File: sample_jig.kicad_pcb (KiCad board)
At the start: 2 copper layers, 50 x 50 mm, 25 parts

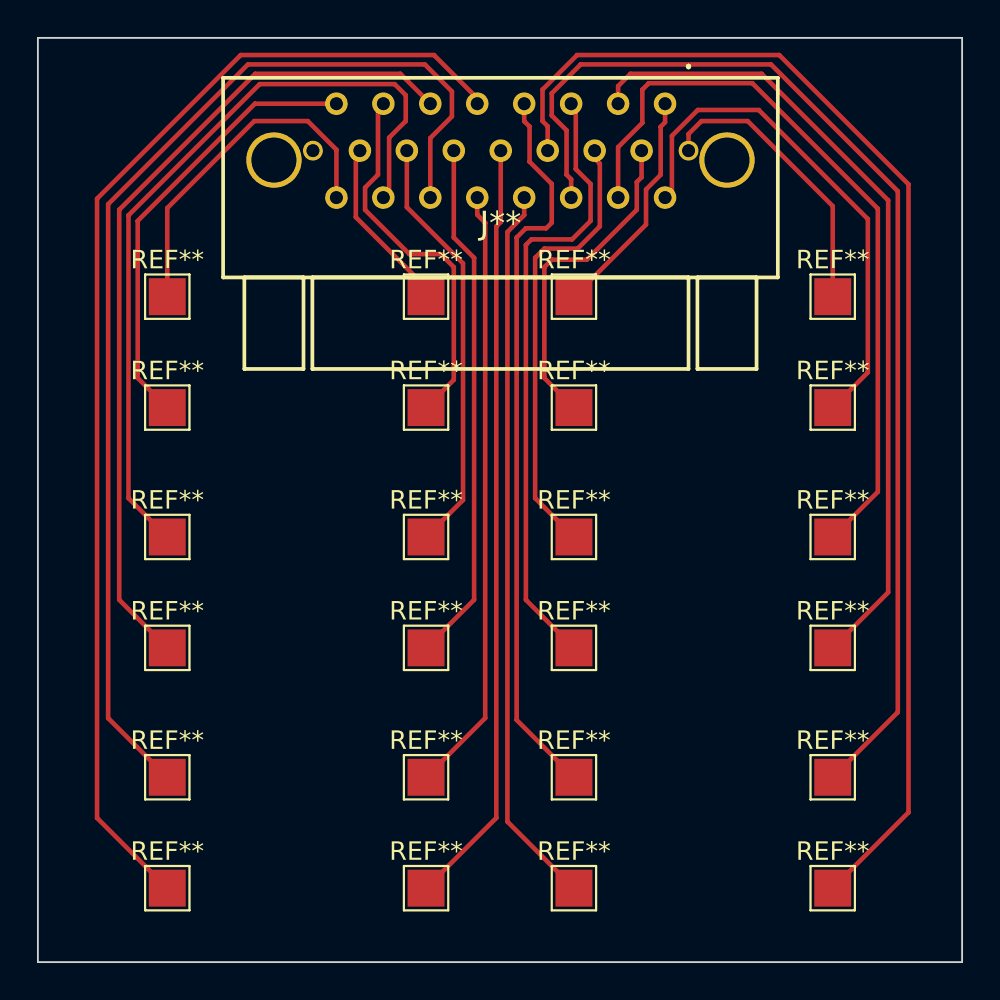
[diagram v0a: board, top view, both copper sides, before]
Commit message: running into some problems with pcb potentially, need to decide if this design will work or to do the more traditional flexing design.
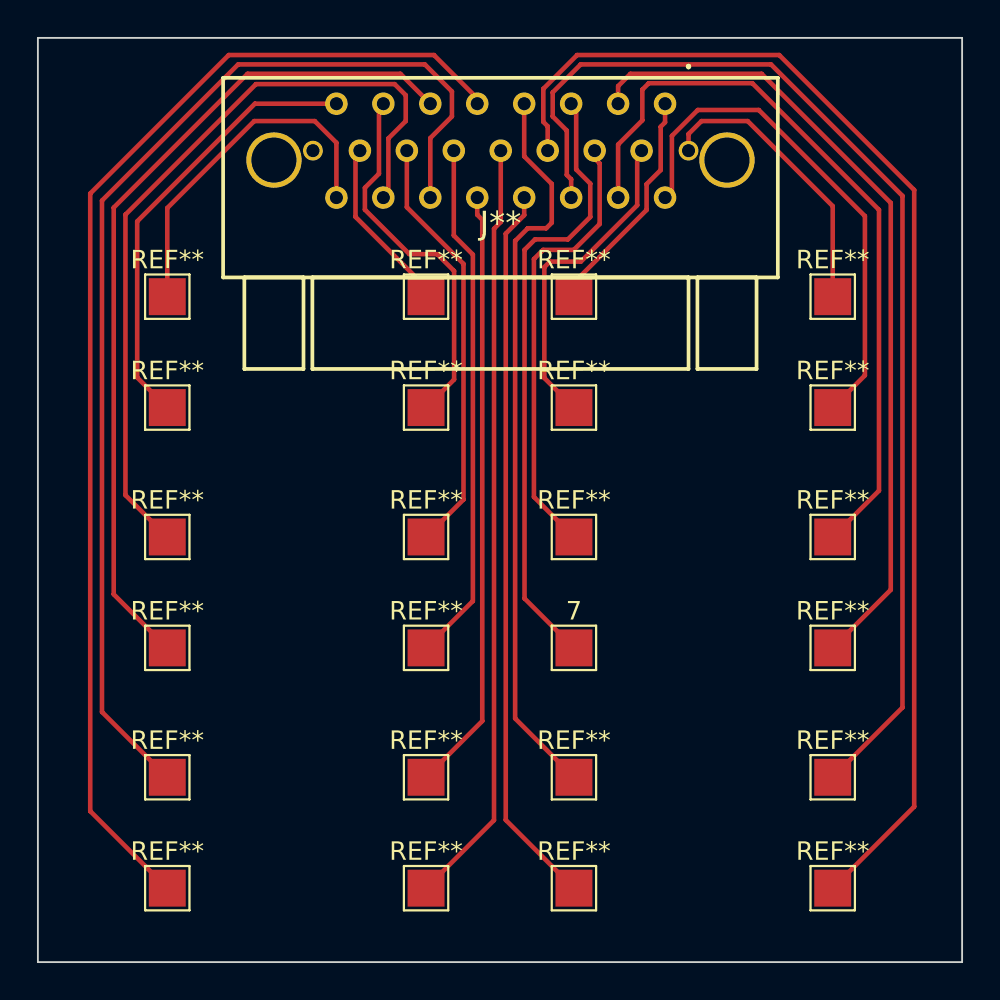
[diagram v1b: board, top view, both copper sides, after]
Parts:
- removed the REF** at (79.0, 83.0)
- added 7: TestPoint_Pad_2.0x2.0mm, TestPoint:TestPoint_Pad_2.0x2.0mm, F.Cu at (79.0, 83.0)
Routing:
- net (no net): track 836.2 -> 838.3 mm

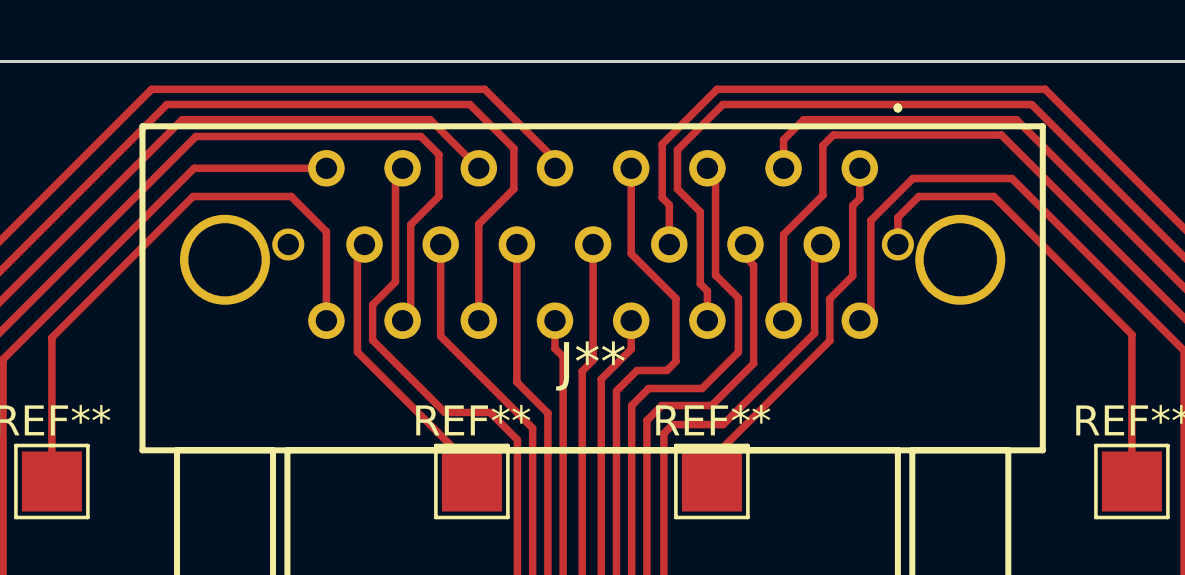
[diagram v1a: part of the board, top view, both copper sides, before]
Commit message: still working on the PCB, modified the drill holes for mounting the microD connector so they shouldn't interfere witht eh plated through holes.
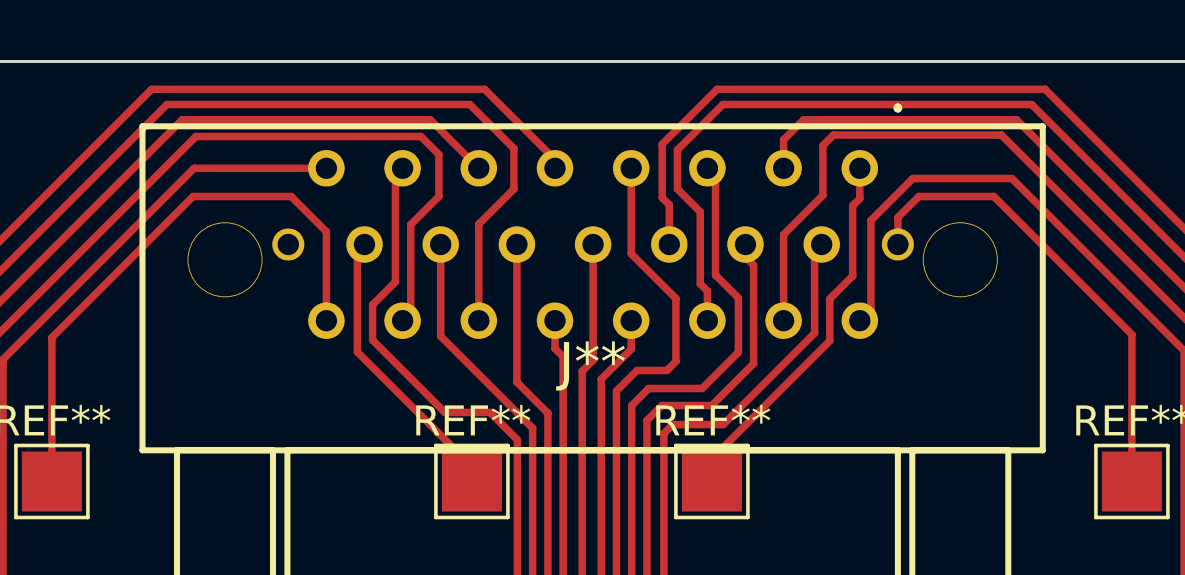
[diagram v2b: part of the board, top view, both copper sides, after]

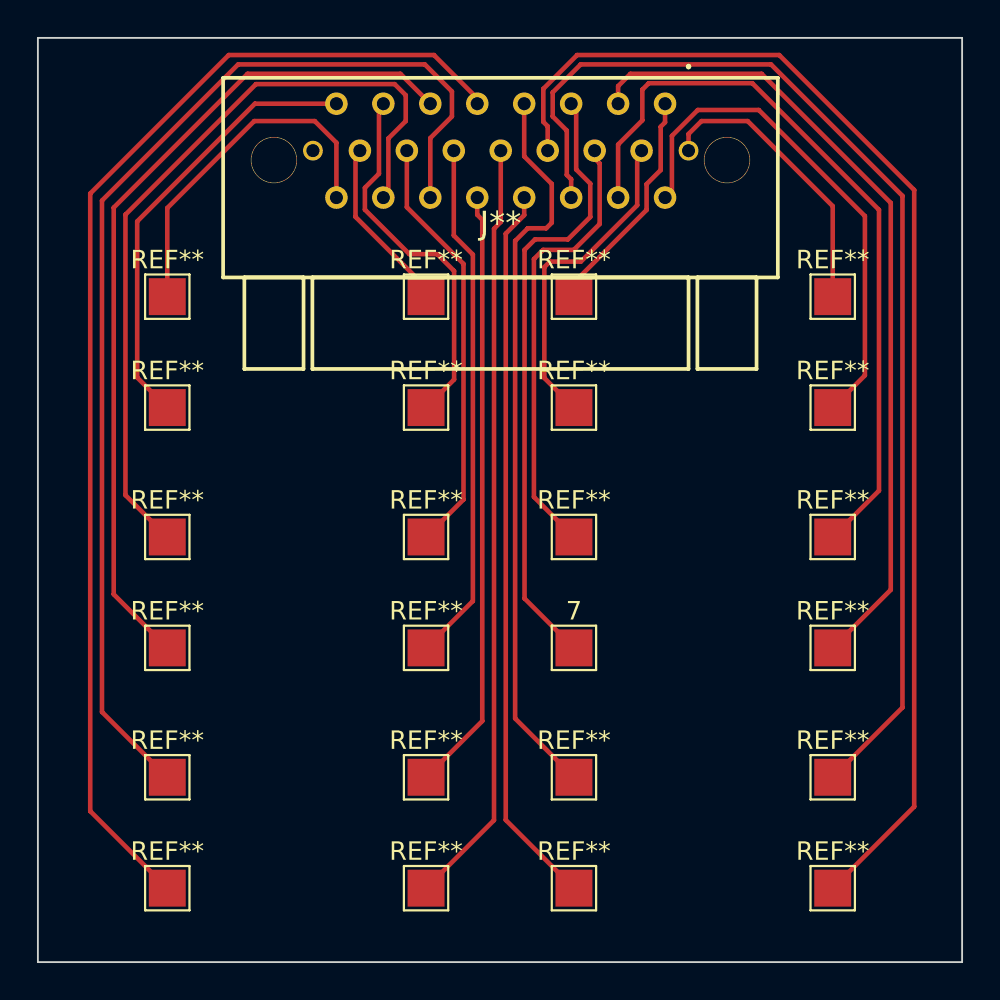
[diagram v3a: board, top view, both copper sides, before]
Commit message: modified the pads to be larger and have double checked all of the traces are the right distance apart (10 mill minimum). I think the last thing i will check is the solder mask for the mounting holes and through holes, it is showing up as the same color as the copper layers, let's take a look at the actual gerber files to get a better comparison.
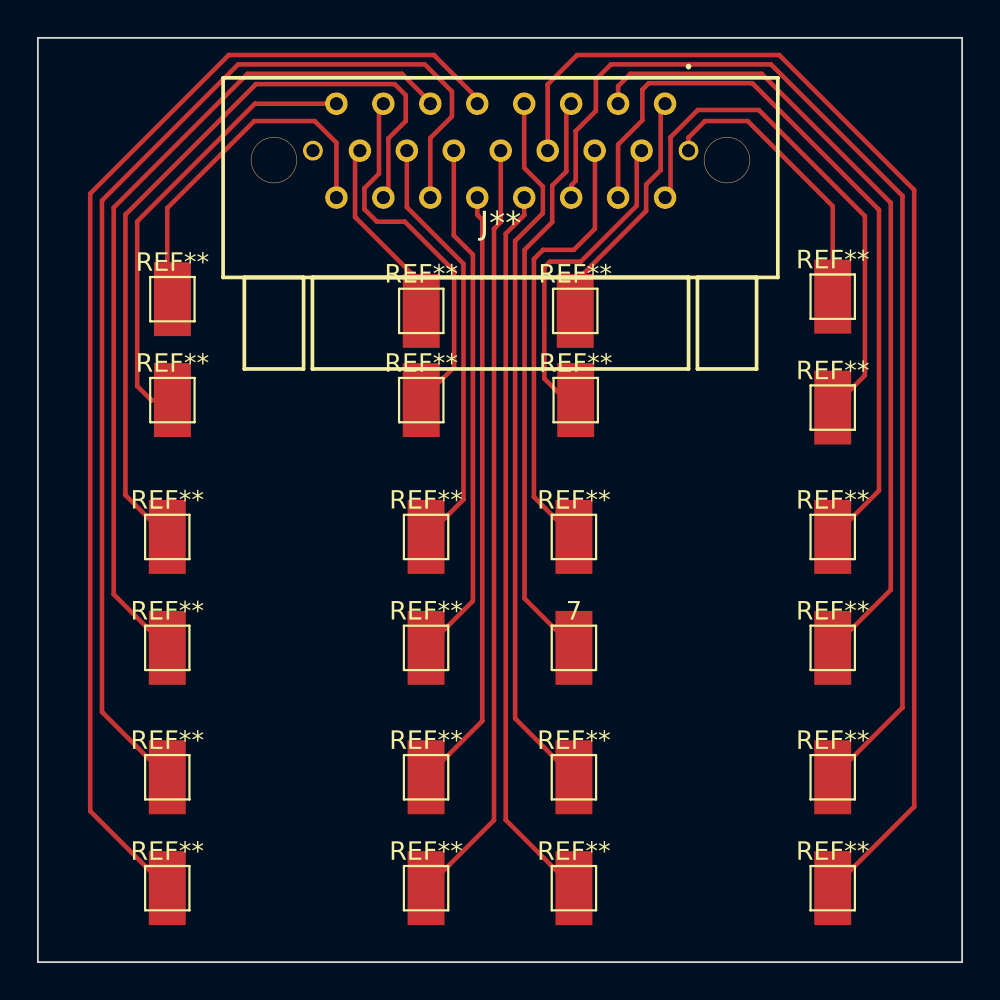
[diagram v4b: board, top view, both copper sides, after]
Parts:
- removed the REF** at (79.0, 70.0)
- removed the REF** at (79.0, 64.0)
- removed the REF** at (71.0, 70.0)
- removed the REF** at (71.0, 64.0)
- added REF**: TestPoint_Pad_2.0x2.0mm, TestPoint:TestPoint_Pad_2.0x2.0mm, F.Cu at (79.1, 69.6)
- added REF**: TestPoint_Pad_2.0x2.0mm, TestPoint:TestPoint_Pad_2.0x2.0mm, F.Cu at (79.1, 64.8)
- added REF**: TestPoint_Pad_2.0x2.0mm, TestPoint:TestPoint_Pad_2.0x2.0mm, F.Cu at (70.7, 69.6)
- added REF**: TestPoint_Pad_2.0x2.0mm, TestPoint:TestPoint_Pad_2.0x2.0mm, F.Cu at (70.7, 64.8)
- moved REF** 0.49 mm to (57.3, 69.6)
- moved REF** 0.31 mm to (57.3, 64.1)
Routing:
- net (no net): track 838.3 -> 835.4 mm

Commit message: finalized version of the board for cirexx
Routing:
- net (no net): track 835.4 -> 834.4 mm
